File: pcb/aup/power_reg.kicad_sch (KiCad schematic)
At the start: 0 parts

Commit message: Start of fpga voltage rails. Added 1v0/vccint
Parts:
- added C301, C302: 10uf/50V, Capacitor_SMD:C_0805_2012Metric, symbol !Misc:C_10uf_0805
- added C303: 0.1uf/50v, Capacitor_SMD:C_0603_1608Metric, symbol !Misc:C_0.1uf_0603
- added C305: 22uf/25V, Capacitor_SMD:C_0805_2012Metric, symbol !Misc:C_22uf_0805
- added L301: 1nH/2A, Inductor_SMD:L_1008_2520Metric, symbol !Misc:L_1uh_3A
- added R301: 150K, Resistor_SMD:R_0603_1608Metric, symbol !Misc:R_150K_0603
- added R302: 51K, Resistor_SMD:R_0603_1608Metric, symbol !Misc:R_51K_0603
- added R303, R305: 10K, Resistor_SMD:R_0603_1608Metric, symbol !Misc:R_10K_0603
- added R304: 15K, Resistor_SMD:R_0603_1608Metric, symbol !Misc:R_15K_0603
- added U301: TPS563257DRLR, Package_TO_SOT_SMD:SOT-563, symbol !Misc:TPS563257DRLR
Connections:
- new net: R304.1, R305.2, U301.6 (FB)
- new net: C301.1, C302.1, C303.1, R301.1, U301.1 (VIN)
- new net: R301.2, R302.1, U301.5 (EN)
- new net +1V0: C305.1, L301.2, R303.2, R305.1
- new net 1V_SW: L301.1, U301.2 (SW)
- new net GND: C301.2, C302.2, C303.2, C305.2, R302.2, R304.2, U301.3 (GND)
- new net PG_1V: R303.1, U301.4 (PG)

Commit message: Finished voltage rail schematic
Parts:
- added C304, C306, C321, C322, C325, C326, C328, C329, C330, C333, C343, C346: 10uf/50V, Capacitor_SMD:C_0805_2012Metric, symbol !Misc:C_10uf_0805
- added C307, C323, C327, C331, C344, C347: 0.1uf/50v, Capacitor_SMD:C_0603_1608Metric, symbol !Misc:C_0.1uf_0603
- added C308, C332, C341, C342, C345, C348: 22uf/25V, Capacitor_SMD:C_0805_2012Metric, symbol !Misc:C_22uf_0805
- added C309, C310, C311, C312, C313, C314, C315: 0.1uf, Capacitor_SMD:C_0402_1005Metric, symbol !Misc:C_0.1uf_0402
- added L302, L303, L304: 2.2uH/2A, Inductor_SMD:L_1008_2520Metric, symbol !Misc:L_2.2uh_3A
- added L306, L307, L308: 1uH/2A, Inductor_SMD:L_1008_2520Metric, symbol !Misc:L_1uh_3A
- added R306, R308, R310, R318, R321, R322, R323, R324, R326: 10K, Resistor_SMD:R_0603_1608Metric, symbol !Misc:R_10K_0603
- added R307, R309, R311, R313: 20K, Resistor_SMD:R_0603_1608Metric, symbol !Misc:R_20K_0603
- added R312, R315: 4.99K, Resistor_SMD:R_0603_1608Metric, symbol !Misc:R_4.99K_0603
- added R314, R316: 15K, Resistor_SMD:R_0603_1608Metric, symbol !Misc:R_15K_0603
- added R317: 43K, Resistor_SMD:R_0603_1608Metric, symbol !Misc:R_43K_0603
- added R319, R320: 51K, Resistor_SMD:R_0603_1608Metric, symbol !Misc:R_51K_0603
- added R325: 30K, Resistor_SMD:R_0603_1608Metric, symbol !Misc:R_30K_0603
- added U302, U306, U307, U308, U311, U312: TPS563257DRLR, SOT6_DRL_TEX, symbol !Misc:TPS563257DRLR
- L301: value 1nH/2A -> 1uH/2A
- U301: footprint Package_TO_SOT_SMD:SOT-563 -> SOT6_DRL_TEX
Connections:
- net GND: now also C304.2, C306.2, C307.2, C308.2, C309.2, C310.2, C311.2, C312.2, C313.2, C314.2, C315.2, C321.2, C322.2, C323.2, C325.2, C326.2, C327.2, C328.2, C329.2, C330.2, C331.2, C332.2, C333.2, C341.2, C342.2, C343.2, C344.2, C345.2, C346.2, C347.2, C348.2, R306.2, R309.2, R310.2, R314.2, R320.2, R326.2, U302.3 (GND), U306.3 (GND), U307.3 (GND), U308.3 (GND), U311.3 (GND), U312.3 (GND)
- net +5V: now reaches C301.1, C302.1, C303.1, R301.1, U301.1 (VIN)
- net +5V: now also C304.1, C306.1, C307.1, C321.1, C322.1, C323.1, C325.1, C326.1, C327.1, C328.1, C329.1, C330.1, C331.1, C333.1, C343.1, C344.1, C346.1, C347.1, U302.1 (VIN), U306.1 (VIN), U307.1 (VIN), U308.1 (VIN), U311.1 (VIN), U312.1 (VIN)
- net +1V0 renamed +Vccint
- net +Vccint: now also C309.1
- net 1V_SW renamed SW_Vccint
- net SW_Vccint: now also L302.1, U302.2 (SW)
- net PG_1V renamed PG_Vccint
- net PG_Vccint: now also U302.5 (EN)
- new net: R315.1, R317.2
- new net: R314.1, R315.2, U311.6 (FB)
- new net: R309.1, R312.2, U307.6 (FB)
- new net: R306.1, R307.2, U302.6 (FB)
- new net: R325.2, R326.1, U312.6 (FB)
- new net: R311.2, R312.1
- new net: R319.2, R320.1, U306.6 (FB)
- new net: R310.1, R313.2, U308.6 (FB)
- new net: R316.2, R325.1
- new net +1V2: C313.1, C342.1, L306.2, R318.2, R319.1
- new net +1V35: C312.1, C341.1, L307.2, R311.1, R321.2
- new net +1V8: C311.1, C332.1, L308.2, R313.1, R324.2
- new net +2V5: C314.1, C345.1, L304.2, R317.1, R322.2
- new net +3V3: C315.1, C348.1, L303.2, R316.1, R323.2
- new net +Vccaux: C308.1, C310.1, L302.2, R307.1, R308.2
- new net PG_1V2: R318.1, U306.4 (PG)
- new net PG_1V35: R321.1, U307.4 (PG)
- new net PG_1V8: R324.1, U308.4 (PG)
- new net PG_2V5: R322.1, U311.4 (PG)
- new net PG_3V3: R323.1, U312.4 (PG)
- new net PG_Vccaux: R308.1, U302.4 (PG), U306.5 (EN), U307.5 (EN), U308.5 (EN), U311.5 (EN), U312.5 (EN)
- new net SW_1V2: L306.1, U306.2 (SW)
- new net SW_1V35: L307.1, U307.2 (SW)
- new net SW_1V8: L308.1, U308.2 (SW)
- new net SW_2V5: L304.1, U311.2 (SW)
- new net SW_3V3: L303.1, U312.2 (SW)
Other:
- note added: "1v8 would ideally use a 1.5uh inductor, but weren't widely available in 1008. 2.2 is used for Vccaux to prioritize lowest ripple. 1uh is used for Vccoo 1.8 for faster transient response. (These also needed to be spearated to not power up a 1v8 io rail at the same time as Vccaux, although, this could have been achieved with a mosfet gated by the Vccaux PG.) Resistors use JLCPCB basic parts only. U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"
- note added: "Inductor selection: L = (Vout × (Vin - Vout)) / (Vin × ΔIL × f_sw) where ΔIL ≈ 0.3 × Iout Feedback resistor selection: Vout = 0.6 × (1 + Rt / Rb) → Rt / Rb = Vout / 0.6 - 1 → Rt = Rb × (Vout / 0.6 - 1) Enable resistor selection: EN max V is 5.5 max. If feeding from a voltage source, use a voltage divider to stay under this max. Venh (enable is true) max: 1.25V Venl (enable is false) min: 0.9V If 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"
- note added: "Vccint (1v0) -> Vccaux (1v8) -> Vccoo (1v2, 1v35, 1v8, 2v5, 3v3)"
- moved on the sheet: C301, C302, C303, C305, L301, R301, R302, R303, R304, R305, U301

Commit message: Added symbols for the major components
It should be possible to do a first pass placement of ICs on the pcb as
a rough fit check.

Most imported footprints are still missing models.
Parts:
- U10: renamed from U308; footprint SOT6_DRL_TEX -> !Misc:SOT6_DRL_TEX
- U4: renamed from U306; footprint SOT6_DRL_TEX -> !Misc:SOT6_DRL_TEX
- U5: renamed from U301; footprint SOT6_DRL_TEX -> !Misc:SOT6_DRL_TEX
- U6: renamed from U311; footprint SOT6_DRL_TEX -> !Misc:SOT6_DRL_TEX
- U7: renamed from U307; footprint SOT6_DRL_TEX -> !Misc:SOT6_DRL_TEX
- U8: renamed from U302; footprint SOT6_DRL_TEX -> !Misc:SOT6_DRL_TEX
- U9: renamed from U312; footprint SOT6_DRL_TEX -> !Misc:SOT6_DRL_TEX
- renumbered C323 to C10, C301 to C11, C302 to C12, C328 to C13, C303 to C14, C343 to C15, C344 to C16, C313 to C17, C342 to C18, C309 to C19, C314 to C20, C325 to C21, C326 to C22, C345 to C23, C305 to C24, C327 to C25, C304 to C26, C306 to C27, C333 to C28, C312 to C29, C346 to C30, C307 to C31, C341 to C32, C347 to C33, C329 to C34, C330 to C35, C331 to C36, C310 to C37, C315 to C38, C348 to C39, C308 to C40, C311 to C41, C332 to C42, C321 to C8, C322 to C9, L306 to L2, L301 to L3, L304 to L4, L307 to L5, L302 to L6, L303 to L7, L308 to L8, R318 to R12, R301 to R13, R302 to R14, R319 to R15, R320 to R16, R303 to R17, R322 to R18, R305 to R19, R304 to R20, R317 to R21, R315 to R22, R314 to R23, R321 to R24, R311 to R25, R312 to R26, R309 to R27, R308 to R28, R323 to R29, R307 to R30, R306 to R31, R316 to R32, R325 to R33, R326 to R34, R324 to R35, R313 to R36, R310 to R37
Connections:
- net SW_Vccint: no longer L6.1, U8.2 (SW)
- new net SW_Vccaux: L6.1, U8.2 (SW)

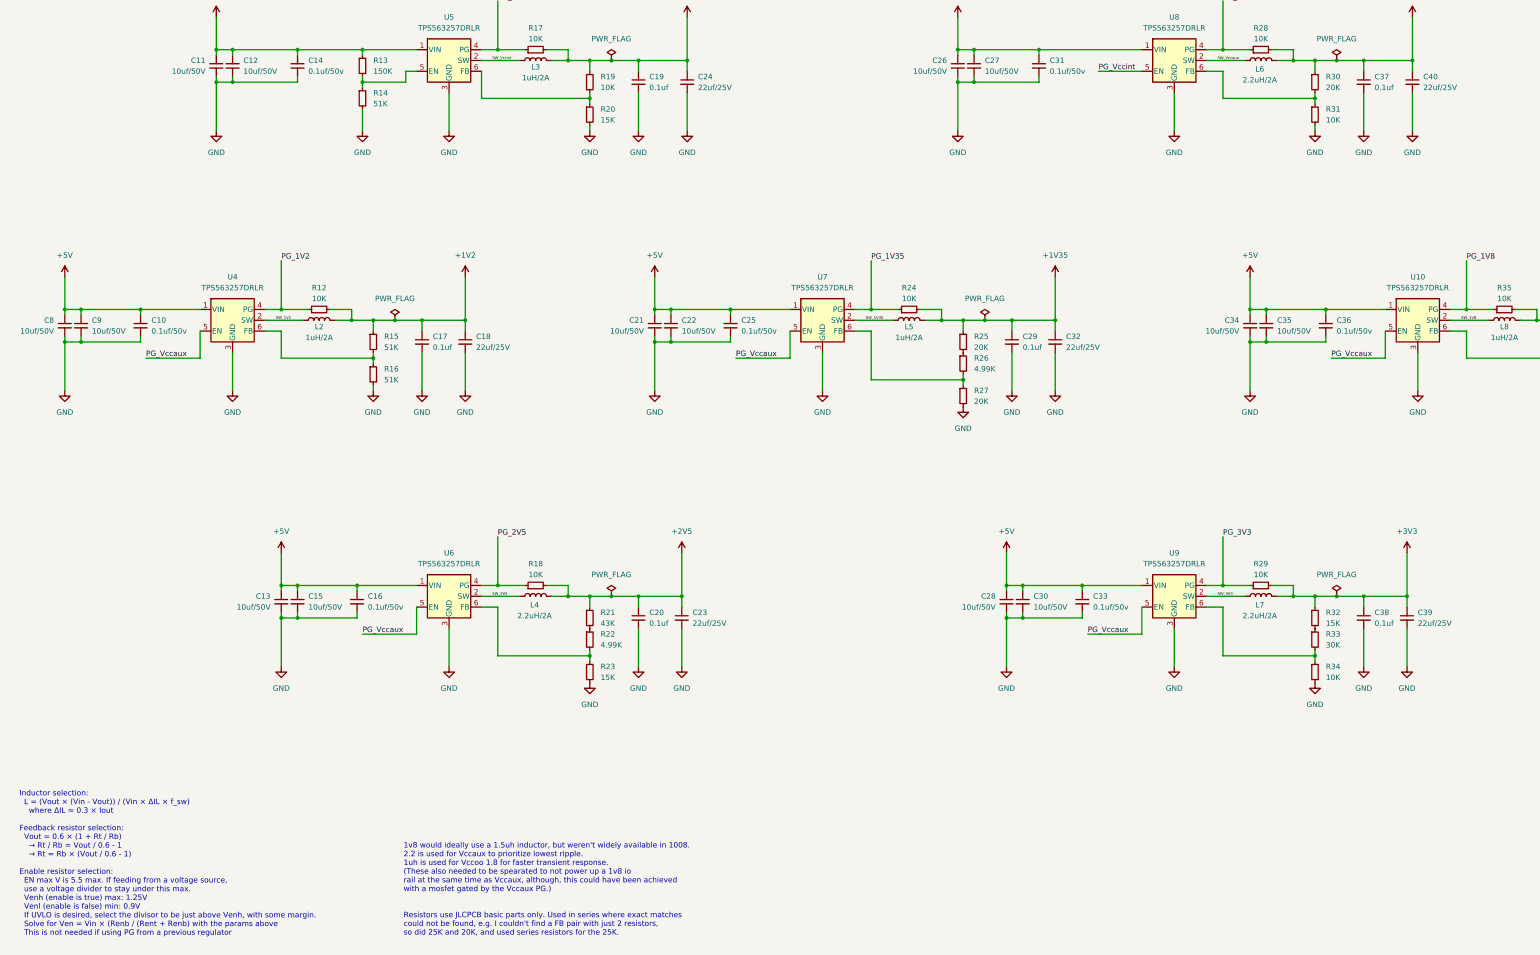
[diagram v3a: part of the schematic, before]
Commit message: Initial layout for Vccint
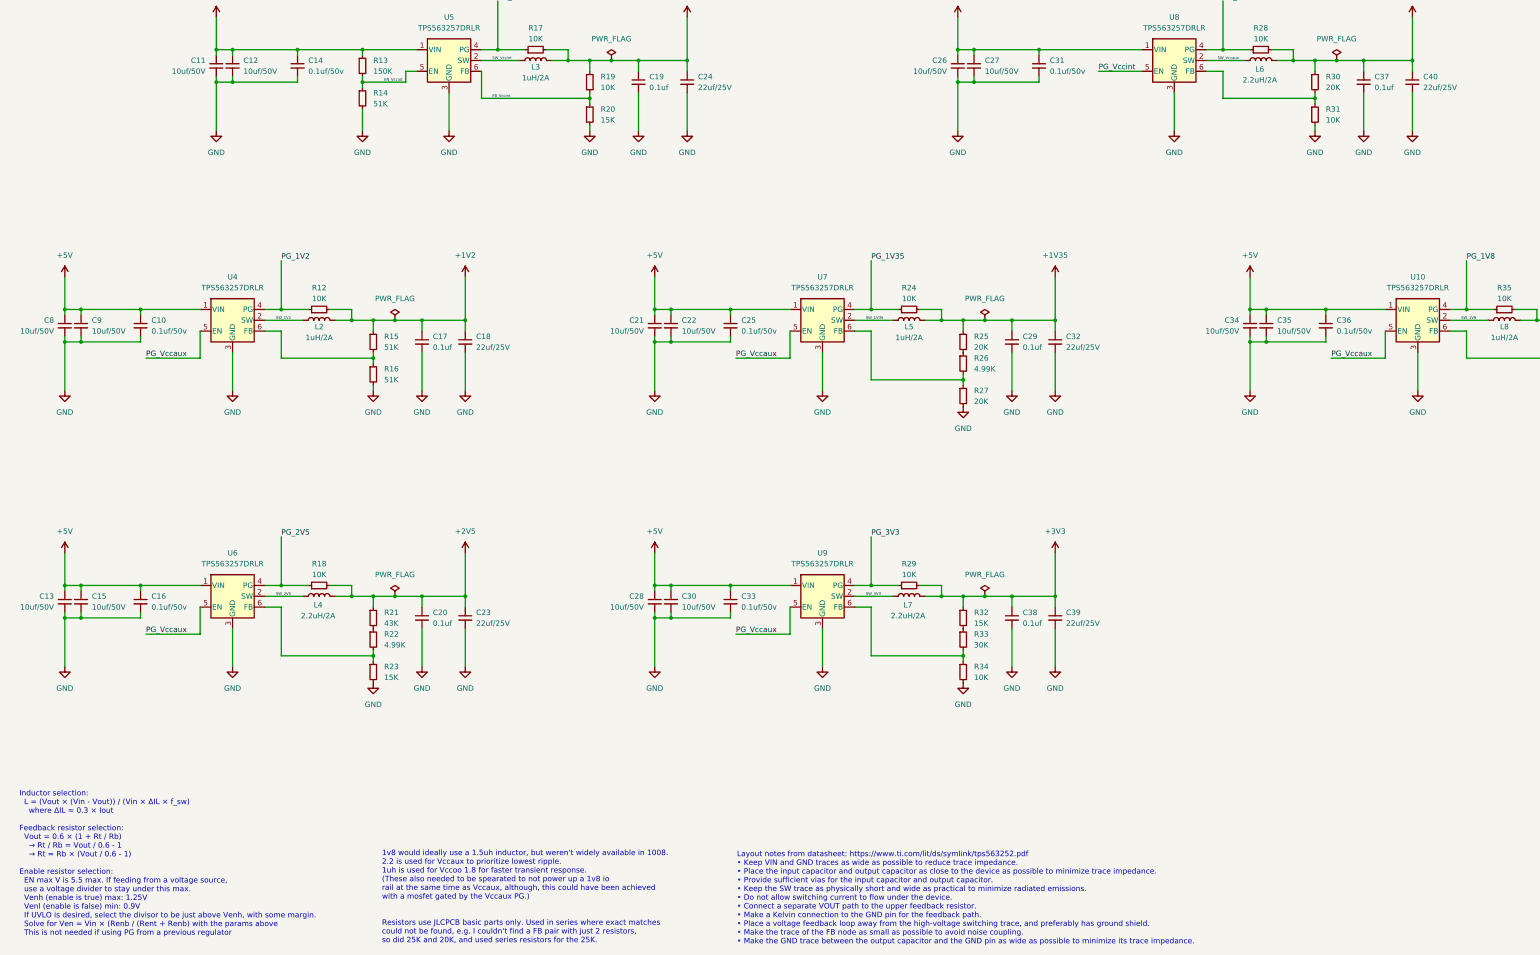
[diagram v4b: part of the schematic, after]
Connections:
- net FB_Vccint: now reaches R19.2, R20.1, U5.6 (FB)
- net EN_Vccint: now reaches R13.2, R14.1, U5.5 (EN)
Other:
- note added: "Layout notes from datasheet: https://www.ti.com/lit/ds/symlink/tps563252.pdf • Keep VIN and GND traces as wide as possible to reduce trace impedance. • Place the input capacitor and output capacitor as close to the device as possible to minimize trace impedance. • Provide sufficient vias for the input capacitor and output capacitor. • Keep the SW trace as physically short and wide as practical to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"
- moved on the sheet: C13, C15, C16, C20, C23, C28, C30, C33, C38, C39, L4, L7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

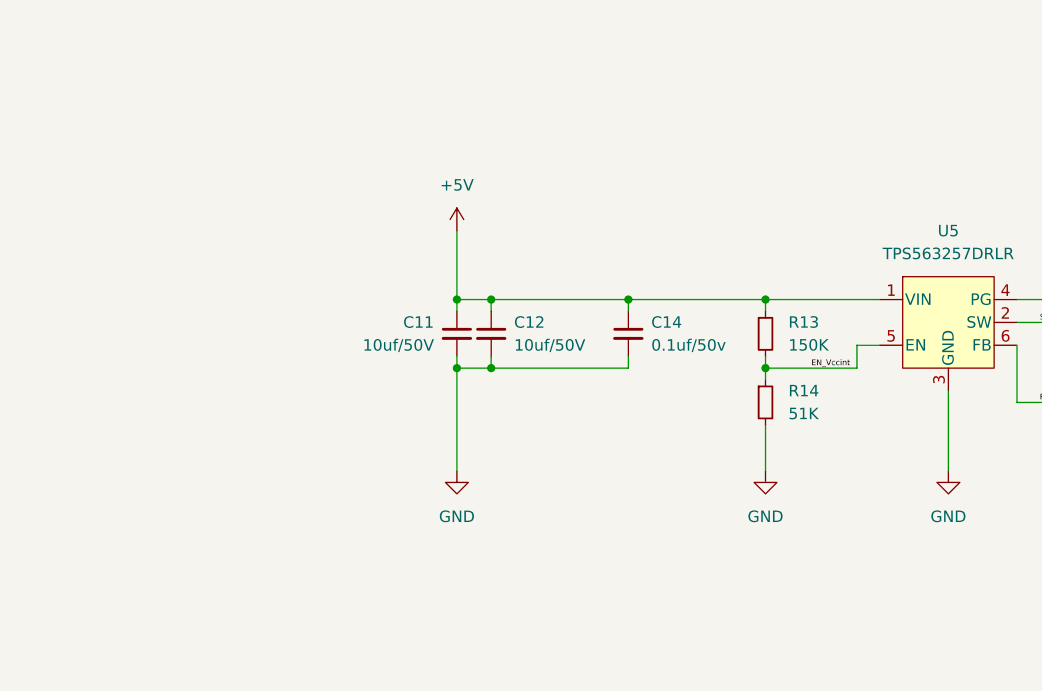
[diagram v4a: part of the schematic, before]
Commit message: First pass on upper voltage rails
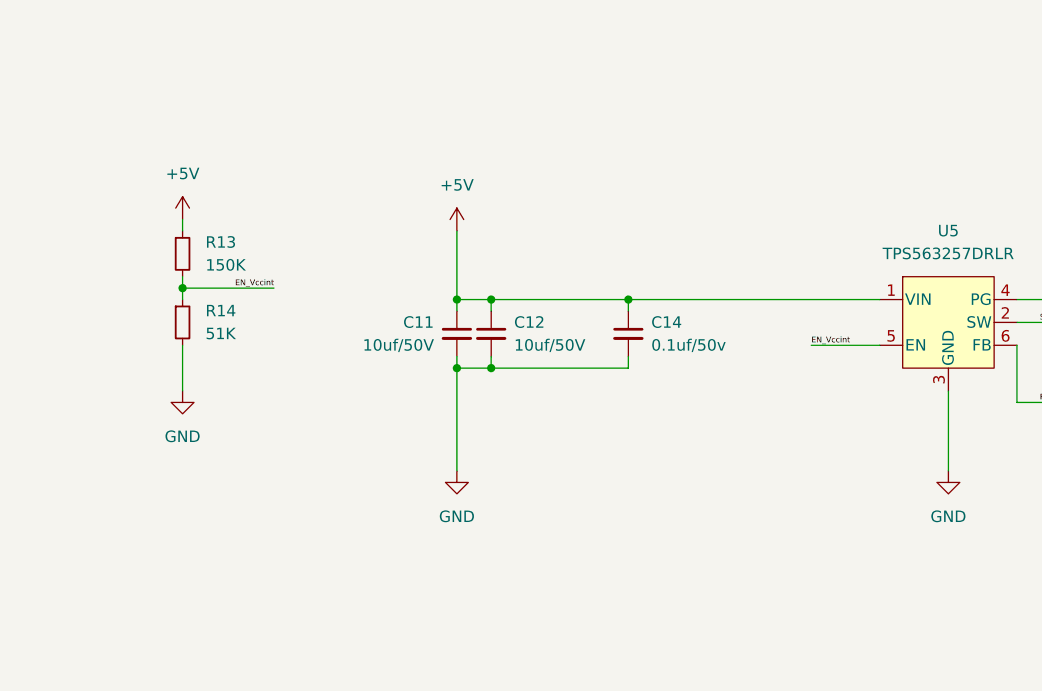
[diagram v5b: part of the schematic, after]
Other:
- moved on the sheet: R13, R14

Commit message: Delete rails that aren't going to be used
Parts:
- removed C13, C15, C34, C35: 10uf/50V, Capacitor_SMD:C_0805_2012Metric, symbol !Misc:C_10uf_0805
- removed C16, C36: 0.1uf/50v, Capacitor_SMD:C_0603_1608Metric, symbol !Misc:C_0.1uf_0603
- removed C20, C41: 0.1uf, Capacitor_SMD:C_0402_1005Metric, symbol !Misc:C_0.1uf_0402
- removed C23, C42: 22uf/25V, Capacitor_SMD:C_0805_2012Metric, symbol !Misc:C_22uf_0805
- removed L4: 2.2uH/2A, Inductor_SMD:L_1008_2520Metric, symbol !Misc:L_2.2uh_3A
- removed L8: 1uH/2A, Inductor_SMD:L_1008_2520Metric, symbol !Misc:L_1uh_3A
- removed R18, R35, R37: 10K, Resistor_SMD:R_0603_1608Metric, symbol !Misc:R_10K_0603
- removed R21: 43K, Resistor_SMD:R_0603_1608Metric, symbol !Misc:R_43K_0603
- removed R22: 4.99K, Resistor_SMD:R_0603_1608Metric, symbol !Misc:R_4.99K_0603
- removed R23: 15K, Resistor_SMD:R_0603_1608Metric, symbol !Misc:R_15K_0603
- removed R36: 20K, Resistor_SMD:R_0603_1608Metric, symbol !Misc:R_20K_0603
- removed U10, U6: TPS563257DRLR, !Misc:SOT6_DRL_TEX, symbol !Misc:TPS563257DRLR
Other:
- note added: "1v8 would ideally use a 1.5uh inductor, but weren't widely available in 1008. 2.2 is used for Vccaux to prioritize lowering ripple over transient response. Resistors use JLCPCB basic parts only. Used in series where exact matches could not be found, e.g. I couldn't find a FB pair with just 2 resistors, so did 25K and 20K, and used series resistors for the 25K."
- note removed: "1v8 would ideally use a 1.5uh inductor, but weren't widely available in 1008. 2.2 is used for Vccaux to prioritize lowest ripple. 1uh is used for Vccoo 1.8 for faster transient response. (These also needed to be spearated to not power up a 1v8 io rail at the same time as Vccaux, although, this could have been achieved with a mosfet gated by the Vccaux PG.) Resistors use JLCPCB basic parts only. U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"
- moved on the sheet: C10, C11, C12, C14, C17, C18, C19, C21, C22, C24, C25, C26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
